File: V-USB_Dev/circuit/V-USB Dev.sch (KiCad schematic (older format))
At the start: 16 parts, among them IC1 ATMEGA8-P, P1 CONN_12, SW1 DIPS_04, X1 16MHz

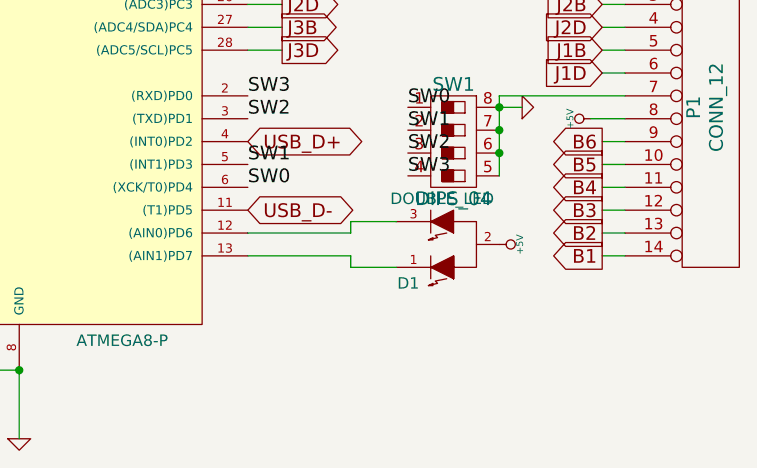
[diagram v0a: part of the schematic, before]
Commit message: * Rename starkadroid circuit to V-USB Dev  * Connect the remaining pins to useful stuff : a dipswitch and a bicolor led.  * Cleanup the schematic to match the hardware  * Also report fixes made on the prototype : connect the free pins on io connector to GND and VCC.
git-svn-id: svn://pulkomandy.tk/avrstuff@48 c6672c3c-f6b6-47f9-9001-1fd6b12fecbe
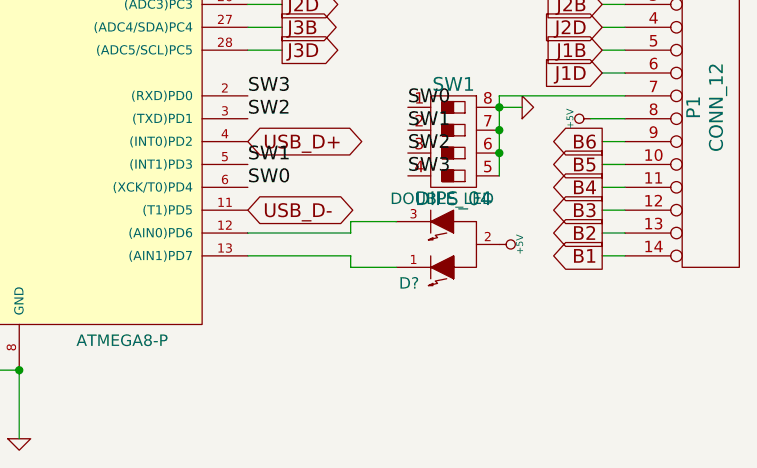
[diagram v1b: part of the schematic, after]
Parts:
- renumbered D1 to D?
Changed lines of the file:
@@
-EESchema Schematic File Version 2  date 05/12/2011 22:52:45
+EESchema Schematic File Version 2  date 05/12/2011 22:35:20
 LIBS:power
 LIBS:device
@@
 $EndDescr
 $Comp
-L +5V #PWR01
+L +5V #PWR?
 U 1 1 4EDD3909
 P 4450 3750
-F 0 "#PWR01" H 4450 3840 20  0001 C CNN
+F 0 "#PWR?" H 4450 3840 20  0001 C CNN
 F 1 "+5V" H 4450 3840 30  0000 C CNN
 	1    4450 3750
@@
 $EndComp
 $Comp
-L DOUBLE_LED D1
+L DOUBLE_LED D?
 U 1 1 4EDD3903
 P 4200 3750
-F 0 "D1" H 4300 3920 50  0000 L CNN
+F 0 "D?" H 4300 3920 50  0000 L CNN
 F 1 "DOUBLE_LED" H 4200 3550 50  0000 C CNN
 	1    4200 3750
@@
 GND
 $Comp
-L +5V #PWR02
+L +5V #PWR01
 U 1 1 4EDD2EFA
 P 1350 1900
-F 0 "#PWR02" H 1350 1990 20  0001 C CNN
+F 0 "#PWR01" H 1350 1990 20  0001 C CNN
 F 1 "+5V" H 1350 1990 30  0000 C CNN
 	1    1350 1900
@@
 SW3
 $Comp
-L +5V #PWR03
+L +5V #PWR02
 U 1 1 4EDD2AC7
 P 4850 3200
-F 0 "#PWR03" H 4850 3290 20  0001 C CNN
+F 0 "#PWR02" H 4850 3290 20  0001 C CNN
 F 1 "+5V" H 4850 3290 30  0000 C CNN
 	1    4850 3200
@@
 $EndComp
 $Comp
-L GND #PWR04
+L GND #PWR03
 U 1 1 4C530791
 P 4550 3150
-F 0 "#PWR04" H 4550 3150 30  0001 C CNN
+F 0 "#PWR03" H 4550 3150 30  0001 C CNN
 F 1 "GND" H 4550 3080 30  0001 C CNN
 	1    4550 3150
@@
 USB_D+
 $Comp
-L +5V #PWR05
+L +5V #PWR04
 U 1 1 4C21EFA8
 P 3900 650
-F 0 "#PWR05" H 3900 740 20  0001 C CNN
+F 0 "#PWR04" H 3900 740 20  0001 C CNN
 F 1 "+5V" H 3900 740 30  0000 C CNN
 	1    3900 650
@@
 $EndComp
 $Comp
-L GND #PWR06
+L GND #PWR05
 U 1 1 4C21EFA1
 P 3850 1550
-F 0 "#PWR06" H 3850 1550 30  0001 C CNN
+F 0 "#PWR05" H 3850 1550 30  0001 C CNN
 F 1 "GND" H 3850 1480 30  0001 C CNN
 	1    3850 1550
@@
 $EndComp
 $Comp
-L GND #PWR07
+L GND #PWR06
 U 1 1 4C20AAB2
 P 2350 4600
-F 0 "#PWR07" H 2350 4600 30  0001 C CNN
+F 0 "#PWR06" H 2350 4600 30  0001 C CNN
 F 1 "GND" H 2350 4530 30  0001 C CNN
 	1    2350 4600
@@
 $EndComp
 $Comp
-L +5V #PWR08
+L +5V #PWR07
 U 1 1 4C20AAA4
 P 2350 1100
-F 0 "#PWR08" H 2350 1190 20  0001 C CNN
+F 0 "#PWR07" H 2350 1190 20  0001 C CNN
 F 1 "+5V" H 2350 1190 30  0000 C CNN
 	1    2350 1100

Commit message: Some fixes and improvements to akusb and lib amiga_keyboard to try not losing that much keypresses. It's not perfect yet, but it's better.
git-svn-id: svn://pulkomandy.tk/avrstuff@49 c6672c3c-f6b6-47f9-9001-1fd6b12fecbe
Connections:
- net B6 is gone; now on net B5: IC1.19 ((SCK)PB5), P1.9 (P9)
- net B1: now also IC1.15 ((OC1A)PB1), P1.13 (P13); no longer IC1.14 ((ICP)PB0), P1.14 (P14)
- net B2: now also IC1.16 ((~SS~/OC1B)PB2), P1.12 (P12); no longer IC1.15 ((OC1A)PB1), P1.13 (P13)
- net B3: now also IC1.17 ((MOSI/OC2)PB3), P1.11 (P11); no longer IC1.16 ((~SS~/OC1B)PB2), P1.12 (P12)
- net B4: now also IC1.18 ((MISO)PB4), P1.10 (P10); no longer IC1.17 ((MOSI/OC2)PB3), P1.11 (P11)
- net B5: no longer IC1.18 ((MISO)PB4), P1.10 (P10)
- net J1B renamed C0
- net J1D renamed C1
- net J2B renamed C2
- net J2D renamed C3
- net J3B renamed C4
- net J3D renamed C5
- new net B0: IC1.14 ((ICP)PB0), P1.14 (P14)
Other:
- note removed: "USB"
- moved on the sheet: D3, D4, R4, R6, R7, USB1
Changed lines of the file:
@@
-EESchema Schematic File Version 2  date 05/12/2011 22:35:20
+EESchema Schematic File Version 2  date 06/12/2011 21:12:27
 LIBS:power
 LIBS:device
@@
 LIBS:contrib
 LIBS:valves
-LIBS:dips-s
-LIBS:w_device
-LIBS:starkadroid-cache
 EELAYER 25  0
 EELAYER END
@@
 Sheet 1 1
 Title "Starkadroid USB Arcade buttons device"
-Date "5 dec 2011"
+Date "6 dec 2011"
 Rev "2010.10.16"
 Comp "PulkoTronics"
@@
 Wire Wire Line
 	1200 1400 1200 1700
-Wire Notes Line
-	3750 1550 3750 1400
-Wire Notes Line
-	3750 1400 2750 1400
-Wire Wire Line
-	4100 1550 4100 1650
-Wire Wire Line
-	3300 1250 3400 1250
-Connection ~ 4000 650
-Wire Wire Line
-	3900 650  4300 650
-Connection ~ 4200 1250
-Wire Wire Line
-	4300 1250 3900 1250
-Connection ~ 4000 1150
-Wire Wire Line
-	4300 1150 3900 1150
+Wire Wire Line
+	4800 1550 4800 1650
+Wire Wire Line
+	4000 1250 4100 1250
+Connection ~ 4700 650
+Wire Wire Line
+	4600 650  5000 650
+Connection ~ 4900 1250
+Wire Wire Line
+	5000 1250 4600 1250
+Connection ~ 4700 1150
+Wire Wire Line
+	5000 1150 4600 1150
 Connection ~ 1900 1150
 Wire Wire Line
@@
 	600  1150 1000 1150
 Connection ~ 600  1150
-Connection ~ 4100 1150
-Wire Wire Line
-	4300 650  4300 1050
-Wire Wire Line
-	3300 1150 3400 1150
-Wire Wire Line
-	4100 1550 3850 1550
-Wire Wire Line
-	4100 1650 4300 1650
-Wire Wire Line
-	4300 1650 4300 1350
-Connection ~ 4200 1650
-Wire Notes Line
-	2750 1400 2750 600
-Wire Notes Line
-	2750 600  4800 600
-Wire Notes Line
-	4800 600  4800 1650
-Wire Notes Line
-	4800 1650 4350 1650
-Wire Notes Line
-	2750 700  2950 700
-Wire Notes Line
-	2950 700  2950 600
+Connection ~ 4800 1150
+Wire Wire Line
+	5000 650  5000 1050
+Wire Wire Line
+	4000 1150 4100 1150
+Wire Wire Line
+	4800 1550 4550 1550
+Wire Wire Line
+	4800 1650 5000 1650
+Wire Wire Line
+	5000 1650 5000 1350
+Connection ~ 4900 1650
 Wire Wire Line
 	600  4300 600  650
@@
 	1    0    0    -1
 $EndComp
-Text Label 4050 3450 0    60   ~ 0
+Text Label 4050 3450 2    60   ~ 0
 SW3
-Text Label 4050 3350 0    60   ~ 0
+Text Label 4050 3350 2    60   ~ 0
 SW2
-Text Label 4050 3250 0    60   ~ 0
+Text Label 4050 3250 2    60   ~ 0
 SW1
-Text Label 4050 3150 0    60   ~ 0
+Text Label 4050 3150 2    60   ~ 0
 SW0
 Text Label 3350 3500 0    60   ~ 0
@@
 $EndComp
 Text GLabel 4900 2600 0    60   Input ~ 0
-J3D
+C5
 Text GLabel 4900 2500 0    60   Input ~ 0
-J3B
+C4
 Text GLabel 4900 2800 0    60   Input ~ 0
-J2D
+C3
 Text GLabel 4900 2700 0    60   Input ~ 0
-J2B
+C2
 Text GLabel 4900 3000 0    60   Input ~ 0
-J1D
+C1
 Text GLabel 4900 2900 0    60   Input ~ 0
-J1B
+C0
 Text GLabel 3500 2900 2    60   Output ~ 0
-J3D
+C5
 Text GLabel 3500 2800 2    60   Output ~ 0
-J3B
+C4
 Text GLabel 3500 2600 2    60   Output ~ 0
-J2B
+C2
 Text GLabel 3500 2700 2    60   Output ~ 0
-J2D
+C3
 Text GLabel 3500 2500 2    60   Output ~ 0
-J1D
+C1
 Text GLabel 3500 2400 2    60   Output ~ 0
-J1B
+C0
 Text GLabel 4900 3300 0    60   Output ~ 0
-B6
+B5
 Text GLabel 4900 3400 0    60   Output ~ 0
+B4
+Text GLabel 4900 3500 0    60   Output ~ 0
+B3
+Text GLabel 4900 3600 0    60   Output ~ 0
+B2
+Text GLabel 4900 3700 0    60   Output ~ 0
+B1
+Text GLabel 4900 3800 0    60   Output ~ 0
+B0
+Text GLabel 3500 2200 2    60   Input ~ 0
 B5
-Text GLabel 4900 3500 0    60   Output ~ 0
+Text GLabel 3500 2100 2    60   Input ~ 0
 B4
-Text GLabel 4900 3600 0    60   Output ~ 0
+Text GLabel 3500 2000 2    60   Input ~ 0
 B3
-Text GLabel 4900 3700 0    60   Output ~ 0
+Text GLabel 3500 1900 2    60   Input ~ 0
 B2
-Text GLabel 4900 3800 0    60   Output ~ 0
+Text GLabel 3500 1800 2    60   Input ~ 0
 B1
-Text GLabel 3500 2200 2    60   Input ~ 0
-B6
-Text GLabel 3500 2100 2    60   Input ~ 0
-B5
-Text GLabel 3500 2000 2    60   Input ~ 0
-B4
-Text GLabel 3500 1900 2    60   Input ~ 0
-B3
-Text GLabel 3500 1800 2    60   Input ~ 0
-B2
 Text GLabel 3500 1700 2    60   Input ~ 0
-B1
+B0
 $Comp
 L CONN_14 P1
@@
 	0    1    1    0
 $EndComp
-Text Notes 2950 700  2    60   ~ 0
-USB
 $Comp
 L ZENER D4
 U 1 1 4C21F047
-P 4200 1450
-F 0 "D4" H 4150 1200 50  0000 C CNN
-F 1 "3.6V" H 4150 1300 40  0000 C CNN
-	1    4200 1450
+P 4900 1450
+F 0 "D4" H 4850 1200 50  0000 C CNN
+F 1 "3.6V" H 4850 1300 40  0000 C CNN
+	1    4900 1450
 	0    -1   -1   0
 $EndComp
@@
 L ZENER D3
 U 1 1 4C21F044
-P 4100 1350
-F 0 "D3" H 4100 1450 50  0000 C CNN
-F 1 "3.6V" H 4100 1550 40  0000 C CNN
-	1    4100 1350
+P 4800 1350
+F 0 "D3" H 4800 1450 50  0000 C CNN
+F 1 "3.6V" H 4800 1550 40  0000 C CNN
+	1    4800 1350
 	0    -1   -1   0
 $EndComp
@@
 L R R4
 U 1 1 4C21F015
-P 4000 900
-F 0 "R4" V 4080 900 50  0000 C CNN
-F 1 "2.2KR" V 4000 900 50  0000 C CNN
-	1    4000 900
+P 4700 900
+F 0 "R4" V 4780 900 50  0000 C CNN
+F 1 "2.2KR" V 4700 900 50  0000 C CNN
+	1    4700 900
 	1    0    0    -1
 $EndComp
@@
 L R R7
 U 1 1 4C21EFE9
-P 3650 1250
-F 0 "R7" V 3730 1250 50  0000 C CNN
-F 1 "68R" V 3650 1250 50  0000 C CNN
-	1    3650 1250
+P 4350 1250
+F 0 "R7" V 4430 1250 50  0000 C CNN
+F 1 "68R" V 4350 1250 50  0000 C CNN
+	1    4350 1250
 	0    1    1    0
 $EndComp
@@
 L R R6
 U 1 1 4C21EFE5
-P 3650 1150
-F 0 "R6" V 3550 1150 50  0000 C CNN
-F 1 "68R" V 3650 1150 50  0000 C CNN
-	1    3650 1150
-	0    1    1    0
-$EndComp
-Text GLabel 3300 1150 0    60   BiDi ~ 0
+P 4350 1150
+F 0 "R6" V 4250 1150 50  0000 C CNN
+F 1 "68R" V 4350 1150 50  0000 C CNN
+	1    4350 1150
+	0    1    1    0
+$EndComp
+Text GLabel 4000 1150 0    60   BiDi ~ 0
 USB_D-
-Text GLabel 3300 1250 0    60   BiDi ~ 0
+Text GLabel 4000 1250 0    60   BiDi ~ 0
 USB_D+
 $Comp
 L +5V #PWR04
 U 1 1 4C21EFA8
-P 3900 650
-F 0 "#PWR04" H 3900 740 20  0001 C CNN
-F 1 "+5V" H 3900 740 30  0000 C CNN
-	1    3900 650
+P 4600 650
+F 0 "#PWR04" H 4600 740 20  0001 C CNN
+F 1 "+5V" H 4600 740 30  0000 C CNN
+	1    4600 650
 	0    -1   -1   0
 $EndComp
@@
 L GND #PWR05
 U 1 1 4C21EFA1
-P 3850 1550
-F 0 "#PWR05" H 3850 1550 30  0001 C CNN
-F 1 "GND" H 3850 1480 30  0001 C CNN
-	1    3850 1550
+P 4550 1550
+F 0 "#PWR05" H 4550 1550 30  0001 C CNN
+F 1 "GND" H 4550 1480 30  0001 C CNN
+	1    4550 1550
 	0    1    1    0
 $EndComp
@@
 L CONN_4 USB1
 U 1 1 4C21EF7A
-P 4650 1200
-F 0 "USB1" V 4600 1200 50  0000 C CNN
-F 1 "CONN_4" V 4700 1200 50  0000 C CNN
-	1    4650 1200
+P 5350 1200
+F 0 "USB1" V 5300 1200 50  0000 C CNN
+F 1 "CONN_4" V 5400 1200 50  0000 C CNN
+	1    5350 1200
 	1    0    0    -1
 $EndComp
